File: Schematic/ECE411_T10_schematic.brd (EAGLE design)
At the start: 76.2 x 62.2 mm, 64 parts, among them IC1 LM386MM-1, J1 1, J2 DCJ0202, J3 AVR_SPI_PRG_6PTH, Q1 8.192 MHz, SW1 SPST_TACT-EVQQ2, U1 ATMEGA328P_PDIP

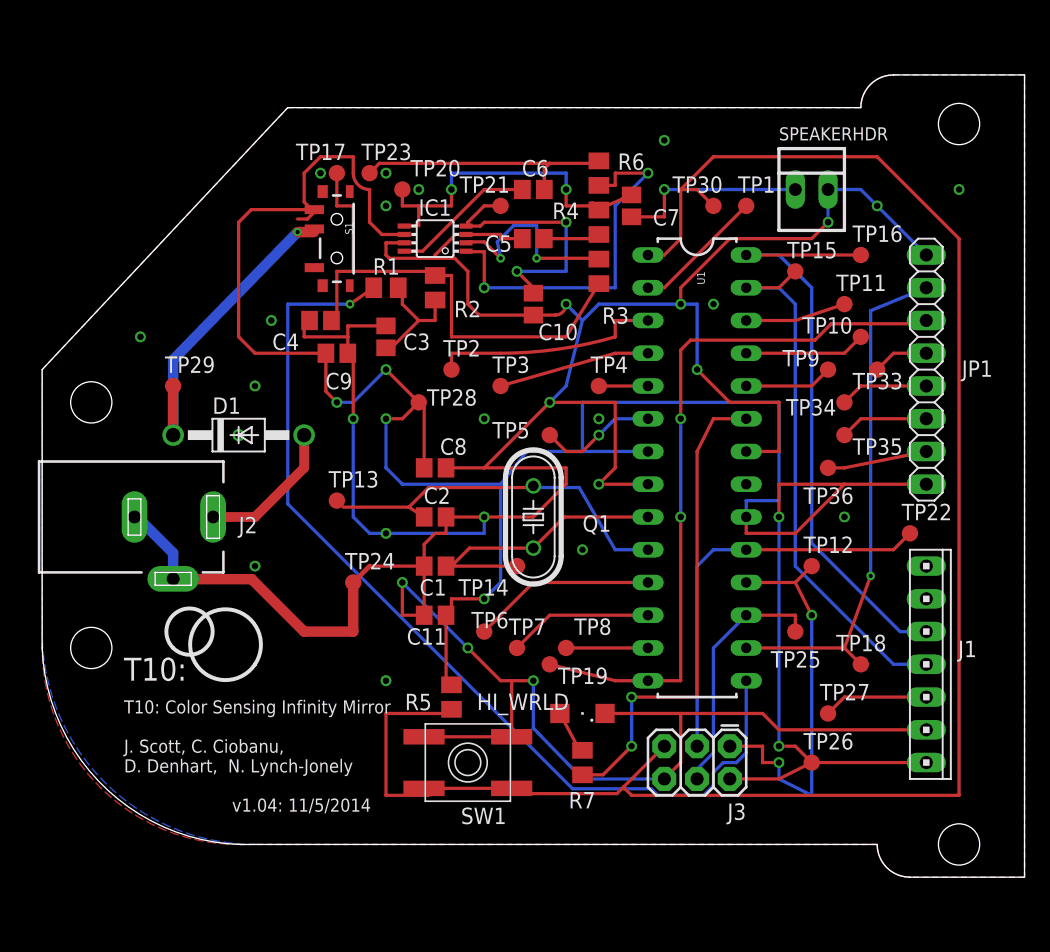
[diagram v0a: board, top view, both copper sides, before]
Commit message: final layout candidate?
- fixed airwire @ (1.30, 1.05)
- smashed/sized some test points on Schematic
- updated dimension layer of board layout for better spacing of mounting
holes
- added team name info to both tPlace and tSilk layers
- png screenshots of final board layout candidate?
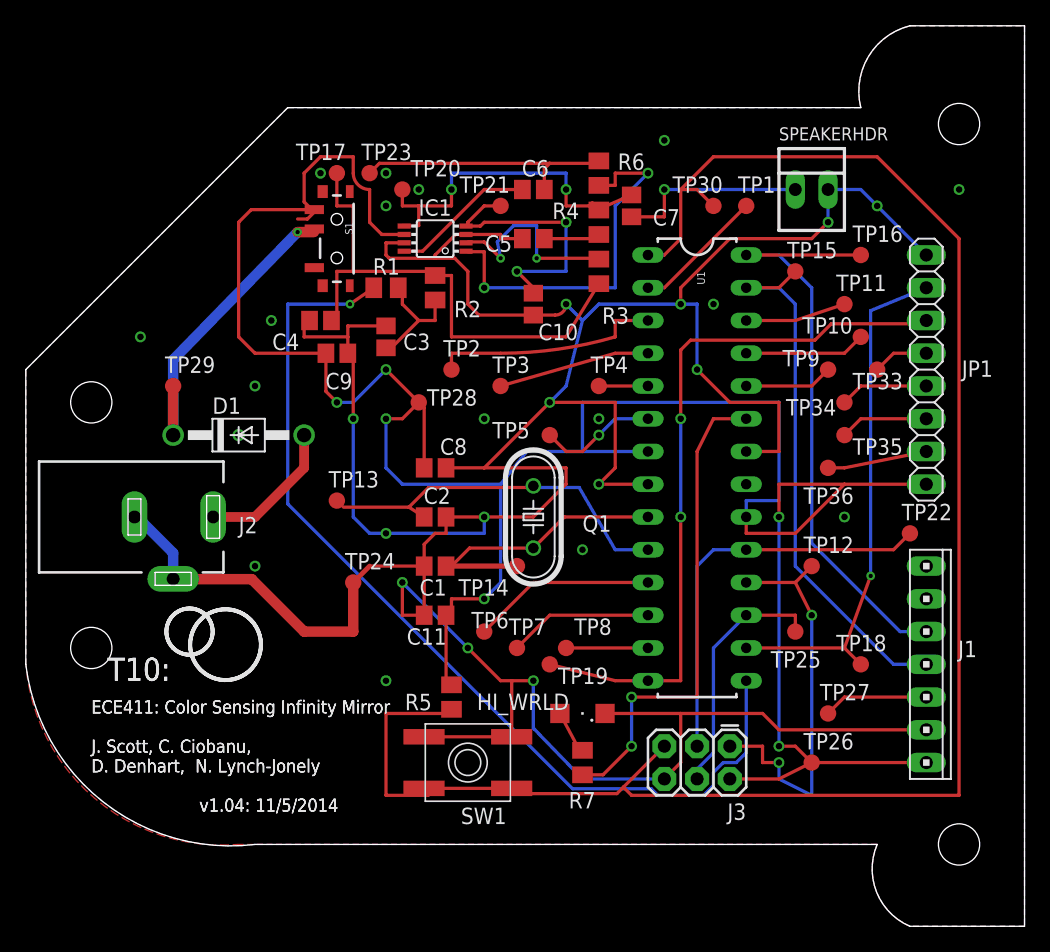
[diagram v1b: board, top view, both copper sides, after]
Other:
- board size 76.2 x 62.2 mm -> 77.5 x 69.8 mm
- board text added: "ECE411: Color Sensing Infinity Mirror J. Scott, C. Ciobanu, D. Denhart, N. Lynch-Jonely v1.04: 11/5/2014"
- board text removed: "T10: Color Sensing Infinity Mirror J. Scott, C. Ciobanu, D. Denhart, N. Lynch-Jonely v1.04: 11/5/2014"
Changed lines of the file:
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@@
 <grid distance="0.05" unitdist="inch" unit="inch" style="lines" multiple="1" display="no" altdistance="0.025" altunitdist="inch" altunit="inch"/>
 <layers>
-<layer number="1" name="Top" color="4" fill="1" visible="no" active="yes"/>
-<layer number="16" name="Bottom" color="1" fill="1" visible="no" active="yes"/>
-<layer number="17" name="Pads" color="2" fill="1" visible="no" active="yes"/>
-<layer number="18" name="Vias" color="2" fill="1" visible="no" active="yes"/>
-<layer number="19" name="Unrouted" color="6" fill="1" visible="no" active="yes"/>
+<layer number="1" name="Top" color="4" fill="1" visible="yes" active="yes"/>
+<layer number="16" name="Bottom" color="1" fill="1" visible="yes" active="yes"/>
+<layer number="17" name="Pads" color="2" fill="1" visible="yes" active="yes"/>
+<layer number="18" name="Vias" color="2" fill="1" visible="yes" active="yes"/>
+<layer number="19" name="Unrouted" color="6" fill="1" visible="yes" active="yes"/>
 <layer number="20" name="Dimension" color="15" fill="1" visible="yes" active="yes"/>
 <layer number="21" name="tPlace" color="7" fill="1" visible="yes" active="yes"/>
 <layer number="22" name="bPlace" color="7" fill="1" visible="no" active="yes"/>
-<layer number="23" name="tOrigins" color="15" fill="1" visible="yes" active="yes"/>
+<layer number="23" name="tOrigins" color="15" fill="1" visible="no" active="yes"/>
 <layer number="24" name="bOrigins" color="15" fill="1" visible="no" active="yes"/>
-<layer number="25" name="tNames" color="7" fill="1" visible="yes" active="yes"/>
+<layer number="25" name="tNames" color="7" fill="1" visible="no" active="yes"/>
 <layer number="26" name="bNames" color="7" fill="1" visible="no" active="yes"/>
 <layer number="27" name="tValues" color="7" fill="1" visible="no" active="yes"/>
 <layer number="28" name="bValues" color="7" fill="1" visible="no" active="yes"/>
-<layer number="29" name="tStop" color="7" fill="3" visible="yes" active="yes"/>
+<layer number="29" name="tStop" color="7" fill="3" visible="no" active="yes"/>
 <layer number="30" name="bStop" color="7" fill="6" visible="no" active="yes"/>
 <layer number="31" name="tCream" color="7" fill="4" visible="no" active="yes"/>
@@
 <board>
 <plain>
-<wire x1="77.47" y1="2.54" x2="77.47" y2="64.77" width="0" layer="20"/>
-<wire x1="77.47" y1="64.77" x2="67.31" y2="64.77" width="0" layer="20"/>
-<wire x1="67.31" y1="64.77" x2="64.77" y2="62.23" width="0" layer="20" curve="90"/>
+<wire x1="77.47" y1="-1.27" x2="77.47" y2="68.58" width="0" layer="20"/>
+<wire x1="77.47" y1="68.58" x2="68.58" y2="68.58" width="0" layer="20"/>
+<wire x1="68.58" y1="68.58" x2="64.77" y2="62.23" width="0" layer="20" curve="90"/>
 <wire x1="64.77" y1="62.23" x2="20.32" y2="62.23" width="0" layer="20"/>
-<wire x1="20.32" y1="62.23" x2="1.27" y2="41.91" width="0" layer="20"/>
-<wire x1="1.27" y1="41.91" x2="1.27" y2="20.32" width="0" layer="20"/>
-<wire x1="66.04" y1="5.08" x2="68.58" y2="2.54" width="0" layer="20" curve="90"/>
-<text x="7.62" y="7.62" size="1.016" layer="112">T10: Color Sensing Infinity Mirror
+<wire x1="20.32" y1="62.23" x2="0" y2="41.91" width="0" layer="20"/>
+<wire x1="0" y1="41.91" x2="0" y2="19.05" width="0" layer="20"/>
+<wire x1="66.04" y1="5.08" x2="68.58" y2="-1.27" width="0" layer="20" curve="90"/>
+<text x="5.08" y="7.62" size="1.016" layer="21">ECE411: Color Sensing Infinity Mirror
 J. Scott, C. Ciobanu,
 D. Denhart,  N. Lynch-Jonely
@@
 <wire x1="13.97" y1="22.86" x2="17.78" y2="19.05" width="0.3048" layer="112" curve="202.619865"/>
 <wire x1="13.97" y1="22.86" x2="11.43" y2="20.32" width="0.3048" layer="112" curve="-180"/>
-<text x="7.62" y="17.78" size="1.778" layer="21">T10:</text>
-<wire x1="68.58" y1="2.54" x2="77.47" y2="2.54" width="0" layer="20"/>
+<text x="6.35" y="17.78" size="1.778" layer="21">T10:</text>
+<wire x1="68.58" y1="-1.27" x2="77.47" y2="-1.27" width="0" layer="20"/>
 <hole x="72.39" y="60.96" drill="3.2"/>
 <hole x="72.39" y="5.08" drill="3.2"/>
@@
 <hole x="5.08" y="20.32" drill="3.2"/>
 <wire x1="66.04" y1="5.08" x2="17.78" y2="5.08" width="0" layer="20"/>
-<wire x1="17.78" y1="5.08" x2="1.27" y2="20.32" width="0" layer="20" curve="-90"/>
+<wire x1="17.78" y1="5.08" x2="0" y2="19.05" width="0" layer="20" curve="-90"/>
+<text x="5.08" y="7.62" size="1.016" layer="112">ECE411: Color Sensing Infinity Mirror
+J. Scott, C. Ciobanu,
+D. Denhart,  N. Lynch-Jonely
+                     v1.04: 11/5/2014</text>
+<wire x1="11.43" y1="20.32" x2="13.97" y2="22.86" width="0.3048" layer="21" curve="-180"/>
+<wire x1="13.97" y1="22.86" x2="17.78" y2="19.05" width="0.3048" layer="21" curve="-157.380135"/>
+<wire x1="13.97" y1="22.86" x2="17.78" y2="19.05" width="0.3048" layer="21" curve="202.619865"/>
+<wire x1="13.97" y1="22.86" x2="11.43" y2="20.32" width="0.3048" layer="21" curve="-180"/>
+<text x="6.35" y="17.78" size="1.778" layer="112">T10:</text>
 </plain>
 <attributes>
@@
 <wire x1="41.91" y1="34.29" x2="35.56" y2="34.29" width="0.254" layer="1"/>
 <polygon width="0.254" layer="1" isolate="0.254">
-<vertex x="1.27" y="41.91"/>
+<vertex x="0" y="41.91"/>
 <vertex x="20.32" y="62.23"/>
 <vertex x="64.77" y="62.23" curve="-90"/>
-<vertex x="67.31" y="64.77"/>
-<vertex x="77.47" y="64.77"/>
-<vertex x="77.47" y="2.54"/>
-<vertex x="68.58" y="2.54" curve="-90"/>
+<vertex x="68.58" y="68.58"/>
+<vertex x="77.47" y="68.58"/>
+<vertex x="77.47" y="-1.27"/>
+<vertex x="68.58" y="-1.27" curve="-90"/>
 <vertex x="66.04" y="5.08"/>
 <vertex x="16.51" y="5.08" curve="-90"/>
-<vertex x="1.27" y="20.32"/>
+<vertex x="0" y="19.05"/>
 </polygon>
 <polygon width="0.254" layer="16" isolate="0.254">
-<vertex x="1.27" y="41.91"/>
+<vertex x="0" y="41.91"/>
 <vertex x="20.32" y="62.23"/>
 <vertex x="64.77" y="62.23" curve="-90"/>
-<vertex x="67.31" y="64.77"/>
-<vertex x="77.47" y="64.77"/>
-<vertex x="77.47" y="2.54"/>
-<vertex x="68.58" y="2.54" curve="-90"/>
+<vertex x="68.58" y="68.58"/>
+<vertex x="77.47" y="68.58"/>
+<vertex x="77.47" y="-1.27"/>
+<vertex x="68.58" y="-1.27" curve="-90"/>
 <vertex x="66.04" y="5.08"/>
 <vertex x="17.78" y="5.08" curve="-90"/>
-<vertex x="1.27" y="21.59"/>
-<vertex x="1.27" y="26.67"/>
+<vertex x="0" y="19.05"/>
 </polygon>
 <via x="66.04" y="54.61" extent="1-16" drill="0.5"/>
@@
 <contactref element="C1" pad="1"/>
 <contactref element="TP14" pad="TP"/>
-<wire x1="32.6" y1="26.67" x2="38.1" y2="26.67" width="0.254" layer="1"/>
 <wire x1="48.26" y1="30.48" x2="41.783" y2="30.48" width="0.254" layer="1"/>
 <wire x1="41.783" y1="30.48" x2="39.37" y2="28.067" width="0.254" layer="1"/>
 <wire x1="39.37" y1="28.067" x2="34.417" y2="28.067" width="0.254" layer="1"/>
 <wire x1="34.417" y1="28.067" x2="33.02" y2="26.67" width="0.254" layer="1"/>
-<wire x1="32.6" y1="26.67" x2="33.02" y2="26.67" width="0" layer="19" extent="1-1"/>
+<wire x1="33.02" y1="26.67" x2="38.1" y2="26.67" width="0.4064" layer="1"/>
+<wire x1="32.6" y1="26.67" x2="33.02" y2="26.67" width="0.4064" layer="1"/>
 </signal>
 <signal name="N$7">

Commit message: more board edits - new pngs
- moved test pad #14 as it was inaccessible
- rerouted R6 R3 R4 for tKeepout
- smash/resized some test points
- updated pngs
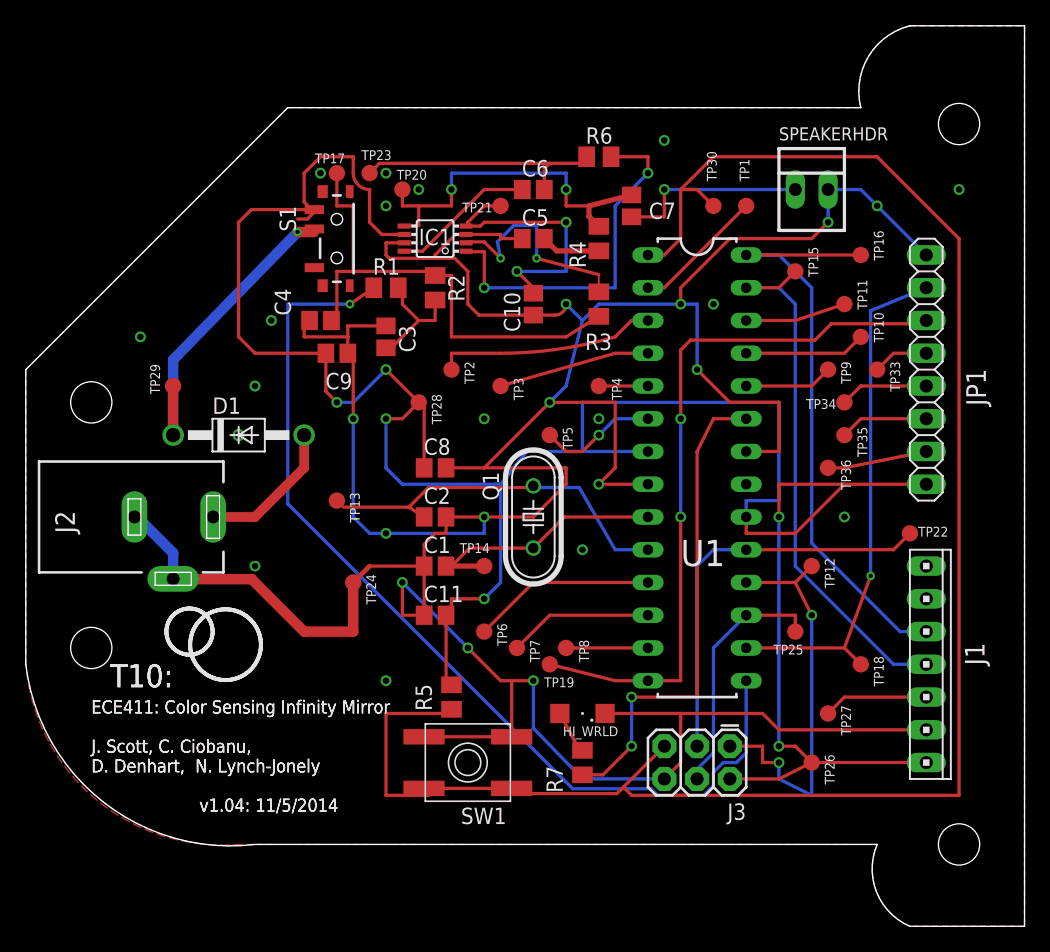
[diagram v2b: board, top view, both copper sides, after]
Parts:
- moved R3 2.54 mm to (44.5, 47.0)
- moved TP14 2.54 mm to (35.6, 26.7)
- moved R4 1.27 mm to (44.5, 52.1)
- moved R6 1.27 mm to (44.5, 58.4), turned to 180 degrees
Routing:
- net N$2: track 22.3 -> 19.8 mm
- net N$6: track 40.7 -> 38.8 mm
- net N$8: track 15.5 -> 17.0 mm
- net N$22: track 17.9 -> 17.1 mm
- net N$3: track 29.1 -> 28.4 mm
- net N$12: track 28.4 -> 29.1 mm
- net N$11: track 20.5 -> 19.9 mm

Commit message: layout/schematic changes
- rerouted INT to PD2
- rerouted LED_FN to PC2
- increased trace size around pad connections
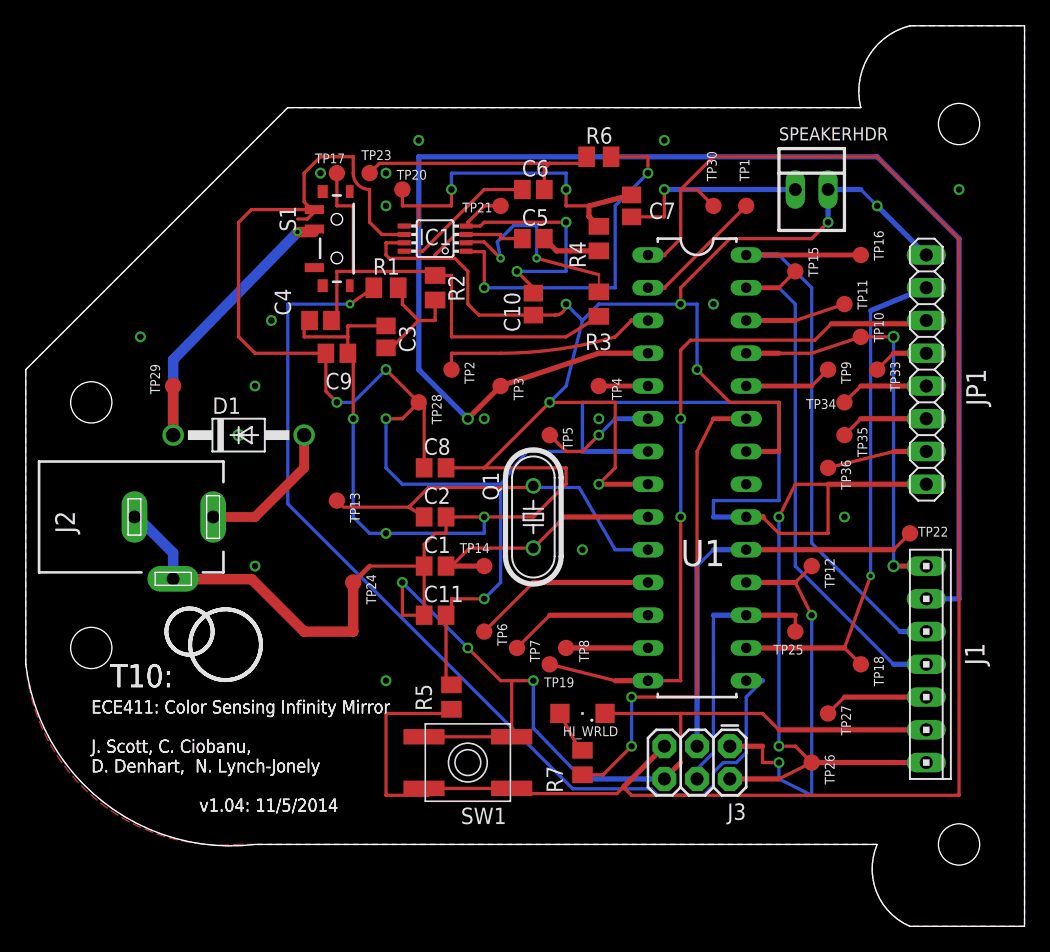
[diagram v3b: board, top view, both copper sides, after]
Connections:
- removed net N$23: TP3.TP, U1.4
- removed net N$29: TP10.TP, U1.25
- net INT: now also TP3.TP, U1.4
- net LED_FN: now also TP10.TP, U1.25
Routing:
- net INT: track 0.00 -> 112.4 mm, vias 0 -> 1
- net LED_FN: track 0.00 -> 32.0 mm, vias 0 -> 2
- net N$23: track 11.8 -> 0.00 mm
- net N$29: track 9.42 -> 0.00 mm
- net VIN: track 197.8 -> 202.2 mm
- net N$4: track 75.0 -> 76.8 mm
- net N$20: track 19.4 -> 20.8 mm
